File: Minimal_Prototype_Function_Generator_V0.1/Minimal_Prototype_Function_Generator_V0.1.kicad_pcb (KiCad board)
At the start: 4 copper layers, 72.3 x 80.6 mm, 170 parts, among them IC1 AD9106BCPZ, IC2 ADP5300ACPZ-1-R7, IC3 ADM7160ACPZN3.3-R7, IC4 LT3472EDD#PBF, IC6 ADM7160ACPZN3.3-R7, IC7 ADM7160ACPZN3.3-R7, IC8 ADM7160ACPZN3.3-R7, IC9 STM32L476VGT6, J1 142-0701-201, J10 SPI_TP_1, J2 142-0701-201, J3 142-0701-201, J4 142-0701-201, J5 142-0701-201, J6 142-0701-201, J7 DEBUG_UART_TP_1, J8 I2C_TP1, J9 USB4500-03-0-A, P5V2_TP1 TestPoint, T1 ADT2-1T+, U1 ADA4817-2ACP, U3 ADA4817-2ACP, Y1 AX3DCF1-156.2500T, Y2 ECS-.327-7-16-C-TR

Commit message: new pcb version
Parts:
- removed D4: SM05.TCT, Insyte_Footprints:SOT95P237X125-3N
- removed FB1, FB2, FB3, FB4: 1.8K OHM AT 100MEGHZ, Inductor_SMD:L_0603_1608Metric
- removed J1, J2, J3, J4, J5, J6: 142-0701-201, Insyte_Footprints:1420701201
- removed JP1, JP2: Jumper_3_Open, Connector_PinHeader_2.54mm:PinHeader_1x03_P2.54mm_Vertical
- removed R4: 100R, Resistor_SMD:R_0603_1608Metric
- removed T1: ADT2-1T+, Insyte_Footprints:ADT21T
- removed U4: ~, Insyte_Logo_Footprints:15x6_Insyte_Logo
- added C70: 100nF, Insyte_Footprints:C_0603, F.Cu at (86.3, 64.8)
- added C71: 100nF, Insyte_Footprints:C_0603, F.Cu at (90.9, 60.6)
- added G***: LOGO, Insyte_Logo_Footprints:20x8_Insyte_Logo, F.Cu at (128.9, 61.6)
- added IC5: TMUXHS221FRSWR, Insyte_Footprints:TMUXHS221FRSWR, F.Cu at (87.9, 60.5)
- added J12: 142-0701-801, Insyte_Footprints:142-0701-851, F.Cu at (103.9, 76.2)
- added J13: 142-0701-801, Insyte_Footprints:142-0701-851, F.Cu at (123.9, 76.2)
- added J14: 142-0701-801, Insyte_Footprints:142-0701-851, F.Cu at (102.9, 39.1)
- added J15: 142-0701-801, Insyte_Footprints:142-0701-851, F.Cu at (122.9, 39.1)
- added J16: 142-0701-801, Insyte_Footprints:142-0701-851, F.Cu at (52.9, 39.1)
- added J17: 142-0701-801, Insyte_Footprints:142-0701-851, F.Cu at (72.9, 39.1)
- added R54: 0R, Insyte_Footprints:R_0603, F.Cu at (39.0, 65.3)
- added R55: 0R, Insyte_Footprints:R_0603, F.Cu at (49.4, 67.7)
- added R56: 0R, Insyte_Footprints:R_0603, F.Cu at (99.0, 60.6)
- added R57: 0R, Insyte_Footprints:R_0603, F.Cu at (96.6, 61.5)
- added R58: 249R, Insyte_Footprints:R_0603, F.Cu at (101.6, 56.0)
- added R59: 39K, Insyte_Footprints:R_0603, F.Cu at (86.3, 63.2)
- added R60: 100R, Insyte_Footprints:R_0603, F.Cu at (101.5, 71.2)
- added R61: 50R, Insyte_Footprints:R_0603, F.Cu at (104.7, 71.2)
- added R62: 100R, Insyte_Footprints:R_0603, F.Cu at (81.4, 60.8)
- added R63: 249R, Insyte_Footprints:R_0603, F.Cu at (74.1, 55.4)
- added R64: 249R, Insyte_Footprints:R_0603, F.Cu at (101.6, 59.1)
- added R65: 249R, Insyte_Footprints:R_0603, F.Cu at (74.1, 58.5)
- added R66: 249R, Insyte_Footprints:R_0603, F.Cu at (99.9, 51.6)
- added R67: 249R, Insyte_Footprints:R_0603, F.Cu at (99.9, 48.5)
- added R68: 249R, Insyte_Footprints:R_0603, F.Cu at (75.9, 51.6)
- added R69: 249R, Insyte_Footprints:R_0603, F.Cu at (75.9, 48.5)
- +3V3_1, +3V3_3, +3V3_5, +3V6_1, +5V_1, N5V2_TP1, P5V2_TP1: footprint TestPoint:TestPoint_Loop_D3.80mm_Drill2.5mm -> Insyte_Footprints:Testpoint_hole; moved to B.Cu
- +3V3_4: footprint TestPoint:TestPoint_Loop_D3.80mm_Drill2.5mm -> Insyte_Footprints:Testpoint_hole
- C1, C10, C17, C18, C24, C9: footprint Capacitor_SMD:C_0603_1608Metric -> Insyte_Footprints:C_0402
- C11, C12, C13, C14, C15, C16, C2, C23, C25, C26, C27, C28, C29, C3, C30, C33, C34, C35, C36, C37, C38, C39, C4, C40, C41, C44, C45, C46, C47, C48, C49, C5, C50, C52, C54, C55, C56, C67, C68: footprint Capacitor_SMD:C_0603_1608Metric -> Insyte_Footprints:C_0603
- C19, C20, C21, C22: footprint Capacitor_SMD:C_0603_1608Metric -> Insyte_Footprints:C_0603; moved to F.Cu
- C31, C32: footprint Capacitor_SMD:C_0603_1608Metric -> Insyte_Footprints:C_0603; moved to B.Cu
- C42, C43, C51, C53, C6, C7, C8: value 0.1uF -> 100nF; footprint Capacitor_SMD:C_0603_1608Metric -> Insyte_Footprints:C_0603
- C57, C58, C59, C60, C61: value 0.1u -> 0.1uF; footprint Capacitor_SMD:C_0603_1608Metric -> Insyte_Footprints:C_0603; moved to B.Cu
- C62: value 4.7u -> 4.7uF; footprint Capacitor_SMD:C_0603_1608Metric -> Insyte_Footprints:C_0603; moved to B.Cu
- C63: value 0.01u -> 0.01uF; footprint Capacitor_SMD:C_0603_1608Metric -> Insyte_Footprints:C_0603; moved to B.Cu
- C64: value 1u -> 1uF; footprint Capacitor_SMD:C_0603_1608Metric -> Insyte_Footprints:C_0603; moved to B.Cu
- C65: value 0.1u -> 0.1uF; footprint Capacitor_SMD:C_0603_1608Metric -> Insyte_Footprints:C_0603
- C66: value 1u -> 1uF; footprint Capacitor_SMD:C_0603_1608Metric -> Insyte_Footprints:C_0603
- D1: footprint LED_SMD:LED_0603_1608Metric -> Insyte_Footprints:CSL1901MW1
- D5, IC9, J10, Y2: moved to B.Cu
- D6: footprint Insyte_Footprints:LEDC1608X85N -> Insyte_Footprints:CSL1901MW1
- L1: value MLP2016H2R2MT0S1 -> MLP2016V2R2MT0S1
- R1, R10, R11, R12, R13, R14, R15, R16, R17, R18, R19, R20, R21, R22, R23, R24, R25, R26, R27, R28, R29, R3, R30, R31, R32, R33, R34, R35, R36, R37, R38, R39, R40, R41, R42, R43, R44, R45, R46, R5, R51, R52, R53, R6, R7, R8, R9: footprint Resistor_SMD:R_0603_1608Metric -> Insyte_Footprints:R_0603
- R2: value 100R -> 5K; footprint Resistor_SMD:R_0603_1608Metric -> Insyte_Footprints:R_0603
- R47, R48, R49, R50: footprint Resistor_SMD:R_0603_1608Metric -> Insyte_Footprints:R_0603; moved to B.Cu
- moved J9 87.1 mm to (57.9, 111.3), turned to 0 degrees
- moved C28 84.3 mm to (39.0, 68.5), turned to -90 degrees
- moved P5V2_TP1 83.5 mm to (39.0, 62.0)
- moved C27 81.8 mm to (41.4, 67.7), turned to 180 degrees
- moved C23 80.7 mm to (37.7, 77.5)
- moved R51 79.9 mm to (53.4, 104.5), turned to 180 degrees
- moved R11 79.9 mm to (41.4, 66.1), turned to 180 degrees
- moved L2 79.7 mm to (39.0, 74.3), turned to 90 degrees
- moved R12 77.1 mm to (46.2, 69.2)
- moved C29 76.5 mm to (46.2, 67.7), turned to 0 degrees
- moved D6 76.4 mm to (67.1, 109.2)
- moved C25 76.0 mm to (43.0, 64.5)
- moved C26 75.4 mm to (43.8, 66.9), turned to 90 degrees
- moved C30 75.4 mm to (49.4, 69.2), turned to 0 degrees
- moved +5V_1 75.1 mm to (53.5, 102.0), turned to 180 degrees
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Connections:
- IC9 pad 35: unconnected-(IC9-PB0-Pad35) -> /Function Generator/CLOCK_EN
- IC9 pad 36: unconnected-(IC9-PB1-Pad36) -> /Function Generator/CLOCK_SEL
- L4 pad 1: /Power/LT3472EDD/P5V2_VP -> /Power/LT3472EDD/N5V2_VN
- L4 pad 3: /Power/LT3472EDD/P5V2_VP -> /Power/LT3472EDD/N5V2_VN
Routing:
- net GND: track 121.9 -> 8.51 mm, vias 326 -> 542
- net /Power/VDD_STM32: track 14.8 -> 111.0 mm
- net /Output_Stage/Op_Amp_1/AMP_OUT: track 82.3 -> 3.73 mm, vias 3 -> 0
- net /Output_Stage/Op_Amp_1/AMP1_OUT: track 73.8 -> 3.62 mm, vias 3 -> 0
- net /Function Generator/CLOCK_SEL: track 0.00 -> 50.5 mm, vias 0 -> 3
- net Net-(J13-Pad1): track 53.5 -> 5.13 mm, vias 2 -> 0
- net /USB_C/D-: track 66.1 -> 18.4 mm
- net /USB_C/D+: track 66.3 -> 19.6 mm
- net /Function Generator/CLOCK_EN: track 0.00 -> 45.0 mm, vias 0 -> 3
- net /Function Generator/SPI_MISO: track 24.7 -> 69.6 mm, vias 2 -> 1
- net /Function Generator/SPI_MOSI: track 26.2 -> 68.7 mm, vias 2 -> 1
- net /Output_Stage/P5V2: track 89.6 -> 131.4 mm, vias 15 -> 8
- net /Function Generator/Trigger_Input_3V3: track 2.98 -> 43.7 mm, vias 0 -> 2
- net /Function Generator/SPI_CLK: track 26.5 -> 65.0 mm, vias 0 -> 2
- net /Output_Stage/N5V2: track 84.0 -> 122.2 mm, vias 8 -> 6
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- added copper zone on F.Cu, net /Power/LT3472EDD/N5V2_VN
- added copper zone on F.Cu, net /Power/LT3472EDD/P5V2_VP
- added copper zone on B.Cu, net /Power/VDD_STM32
- added copper zone on F.Cu, net Net-(IC4-DN)
- added copper zone on F.Cu, net Net-(IC4-FBN)
- added copper zone on F.Cu, net Net-(IC4-FBP)
- added copper zone on F.Cu, net Net-(IC4-SSN)
- added copper zone on F.Cu, net Net-(IC4-SWN)
- added copper zone on F.Cu, net Net-(IC4-SWP)
- removed copper zone on F.Cu, net /Output_Stage/N5V2
- removed copper zone on B.Cu, net /Output_Stage/P5V2
- removed copper zone on F.Cu, net /Power/ADM7160ACPZN3.3_1/+3V6
- removed copper zone on F.Cu, net /Power/VDD_STM32
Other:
- board size 72.3 x 80.6 mm -> 110 x 78 mm
- board text added: "+5V2"
- board text added: "-5V2"
- board text added: "3V6"
- board text added: "5V"
- board text added: "CLK"
- board text added: "CLK_EXT"
- board text added: "CLK_TRIG"
- board text added: "CS"
- board text added: "DBG"
- board text added: "Function Generator V2.0"
- board text added: "I2C"
- board text added: "MISO"
- board text added: "MOSI"
- board text added: "OUT_1"
- board text added: "OUT_2"
- board text added: "OUT_3"
- board text added: "OUT_4"
- board text added: "RUN"
- board text added: "SCL"
- board text added: "SDA"
- board text added: "SPI"
- board text added: "VDDA"
- board text added: "VDDD"
- board text added: "VDDX"
- board text added: "VDD_MCU"
- board text removed: "(AVDD)"
- board text removed: "(CVVDX)"
- board text removed: "(VDD_STM32)"
- board text removed: "AMP1"
- board text removed: "AMP2"
- board text removed: "Debug UART"
- board text removed: "Function generator"
- board text removed: "I2C_SCL"
- board text removed: "I2C_SDA"
- board text removed: "JP1 - clock select for {dblquote}SECONDARY{dblquote} winding JP2 - clock select for {dblquote}SECONDARY_DOT{dblquote} winding (pin 2 and 3 are in the same rectangle)"
- board text removed: "Output 1 (IOUT1)"
- board text removed: "Output 2 (IOUT2)"
- board text removed: "Output 3 (IOUT3)"
- board text removed: "Output 4 (IOUT4)"
- board text removed: "PCB v1.0"
- board text removed: "R49 - boot pull-up"
- board text removed: "R50 - boot pull-down"
- board text removed: "RF transformer External clock supply"
- board text removed: "SPI_CLK"
- board text removed: "SPI_CS"
- board text removed: "SPI_MISO"
- board text removed: "SPI_MOSI"
- board text removed: "Trigger input to function generator"

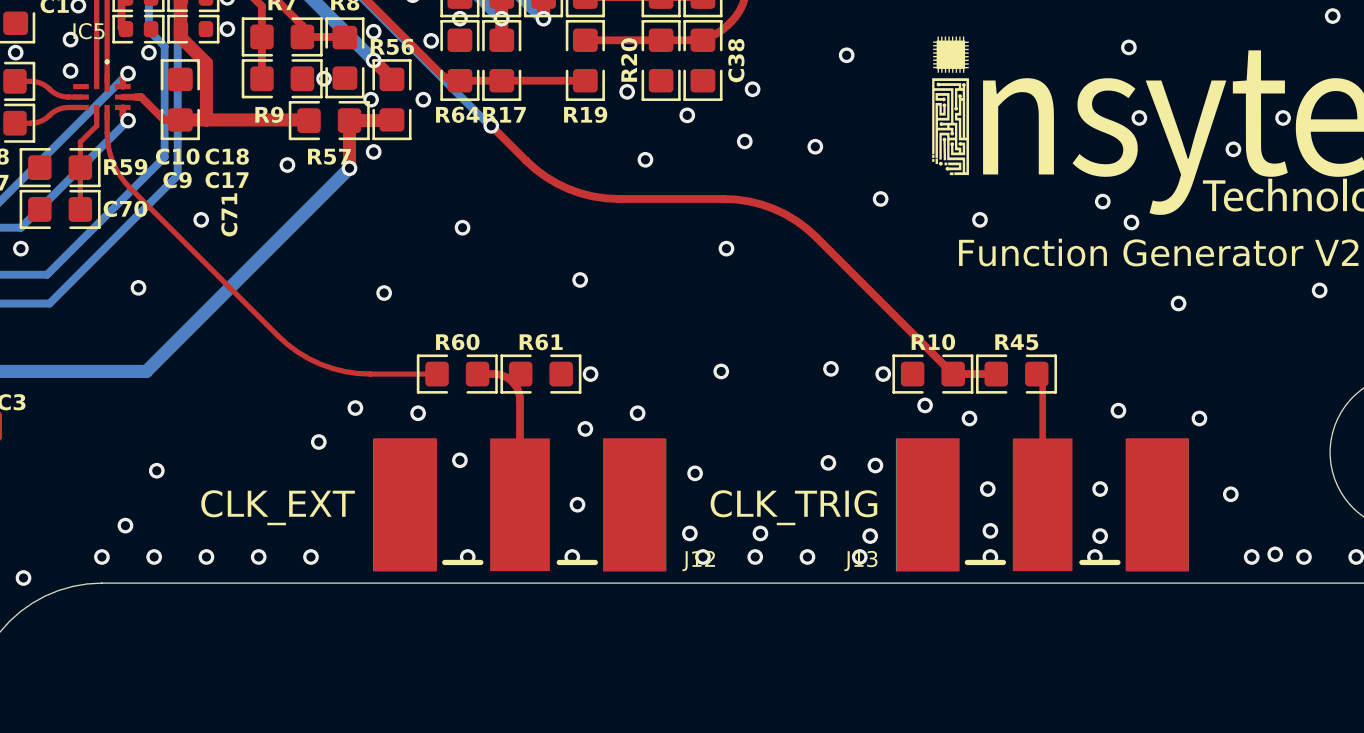
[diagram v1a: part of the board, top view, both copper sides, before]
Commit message: moved SMA connector to make it allign with the top row
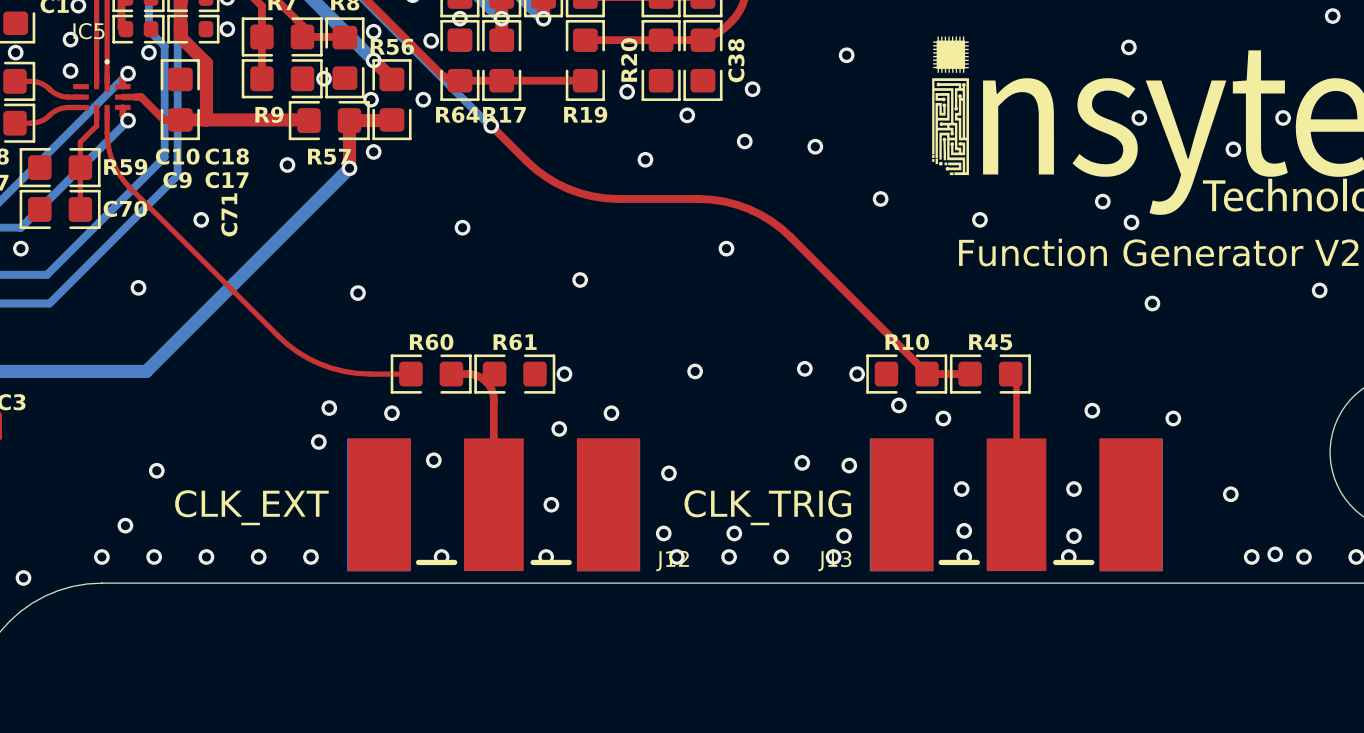
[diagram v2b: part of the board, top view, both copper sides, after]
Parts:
- moved J12 1.00 mm to (102.9, 76.2)
- moved J13 1.00 mm to (122.9, 76.2)
- moved R10 1.00 mm to (118.7, 71.2)
- moved R45 1.00 mm to (121.9, 71.2)
- moved R60 1.00 mm to (100.5, 71.2)
- moved R61 1.00 mm to (103.7, 71.2)
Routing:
- net Net-(IC5-D2+): track 17.6 -> 16.6 mm
- net /Function Generator/Trigger_Input_3V3: track 43.7 -> 42.7 mm

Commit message: V2.0
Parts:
- added C69: 1uF, Insyte_Footprints:C_0603, F.Cu at (125.3, 43.0)
- added C72: 1uF, Insyte_Footprints:C_0603, F.Cu at (75.3, 43.0)
- added C73: 1uF, Insyte_Footprints:C_0603, F.Cu at (100.5, 43.0)
- added C74: 1uF, Insyte_Footprints:C_0603, F.Cu at (50.5, 43.0)
- added R70: 0R, Insyte_Footprints:R_0603, F.Cu at (122.1, 44.5)
- added R71: 0R, Insyte_Footprints:R_0603, F.Cu at (72.1, 44.5)
- added R72: 0R, Insyte_Footprints:R_0603, F.Cu at (103.7, 44.5)
- added R73: 0R, Insyte_Footprints:R_0603, F.Cu at (53.7, 44.5)
- J12, J13, J14, J15, J16, J17: value 142-0701-801 -> SMA-J-P-H-ST-EM1
- R53: value 325R -> 500R
- moved J12 3.00 mm to (102.9, 79.2)
- moved J13 3.00 mm to (122.9, 79.2)
- moved J14 3.00 mm to (102.9, 36.1)
- moved J15 3.00 mm to (122.9, 36.1)
- moved J16 3.00 mm to (52.9, 36.1)
- moved J17 3.00 mm to (72.9, 36.1)
- moved C55 1.80 mm to (52.9, 42.1)
- moved C56 1.80 mm to (72.9, 42.1)
- moved R43 1.61 mm to (56.9, 44.5)
- moved R44 1.61 mm to (68.9, 44.5)
- moved R28 1.61 mm to (118.9, 44.5)
- moved R27 1.60 mm to (106.9, 44.5)
- moved C45 1.50 mm to (102.9, 42.1)
- moved C46 1.40 mm to (122.9, 42.1)
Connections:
- R27 pad 1: Net-(C45-Pad1) -> Net-(R27-Pad1)
- R28 pad 1: Net-(C46-Pad1) -> Net-(R28-Pad1)
- R43 pad 1: Net-(C55-Pad1) -> Net-(R43-Pad1)
- R44 pad 1: Net-(C56-Pad1) -> Net-(R44-Pad1)
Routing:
- net Net-(R44-Pad1): track 0.00 -> 2.00 mm
- net Net-(R43-Pad1): track 0.00 -> 1.67 mm
- net Net-(R28-Pad1): track 0.00 -> 1.65 mm
- net Net-(C45-Pad1): track 1.62 -> 3.27 mm
- net Net-(R27-Pad1): track 0.00 -> 1.65 mm
- net Net-(C56-Pad1): track 1.64 -> 3.27 mm
- net Net-(C46-Pad1): track 1.64 -> 3.27 mm
- net Net-(C55-Pad1): track 1.64 -> 3.26 mm
- net Net-(R28-Pad2): track 12.3 -> 10.8 mm
- net /Output_Stage/P5V2: track 131.4 -> 130.2 mm
- net /Output_Stage/Op_Amp_2/AMP_OUT: track 4.02 -> 3.02 mm
- net /Output_Stage/Op_Amp_2/AMP1_OUT: track 4.02 -> 3.02 mm
- net Net-(R27-Pad2): track 9.10 -> 8.25 mm
- net /Output_Stage/Op_Amp_1/AMP_OUT: track 3.73 -> 3.02 mm
- net Net-(R43-Pad2): track 8.84 -> 8.20 mm
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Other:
- outline, holes or cut-outs redrawn
